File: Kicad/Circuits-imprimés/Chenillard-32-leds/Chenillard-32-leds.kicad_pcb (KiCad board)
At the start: 2 copper layers, 105 x 140 mm, 40 parts, among them J1 Conn_01x02, J2 Conn_01x02, J3 DB25_Female_MountingHoles, J4 DB25_Female_MountingHoles, U1 NE555, U2 4081, U3 4017, U4 4017, U5 4017, U6 4017

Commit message: Update PCB
Update routage and PCB hole mounting
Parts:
- added REF**: M3-Hole, Visserie-Trous-Modules:M3-Hole, F.Cu at (35.0, 40.0)
- added REF**: M3-Hole, Visserie-Trous-Modules:M3-Hole, F.Cu at (35.0, 170.0)
- added REF**: M3-Hole, Visserie-Trous-Modules:M3-Hole, F.Cu at (130.0, 170.0)
- added REF**: M3-Hole, Visserie-Trous-Modules:M3-Hole, F.Cu at (110.0, 50.0)
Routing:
- net RAZ: track 187.5 -> 219.6 mm
- net GND: track 588.8 -> 557.4 mm, vias 7 -> 5
- net Net-(U2-Pad11): track 66.6 -> 54.8 mm
- net Net-(U2-Pad8): track 87.4 -> 94.9 mm
- net +9V: track 428.1 -> 432.8 mm
- net Net-(U2-Pad10): track 58.1 -> 59.2 mm
- net Net-(J3-Pad1): track 44.8 -> 45.8 mm

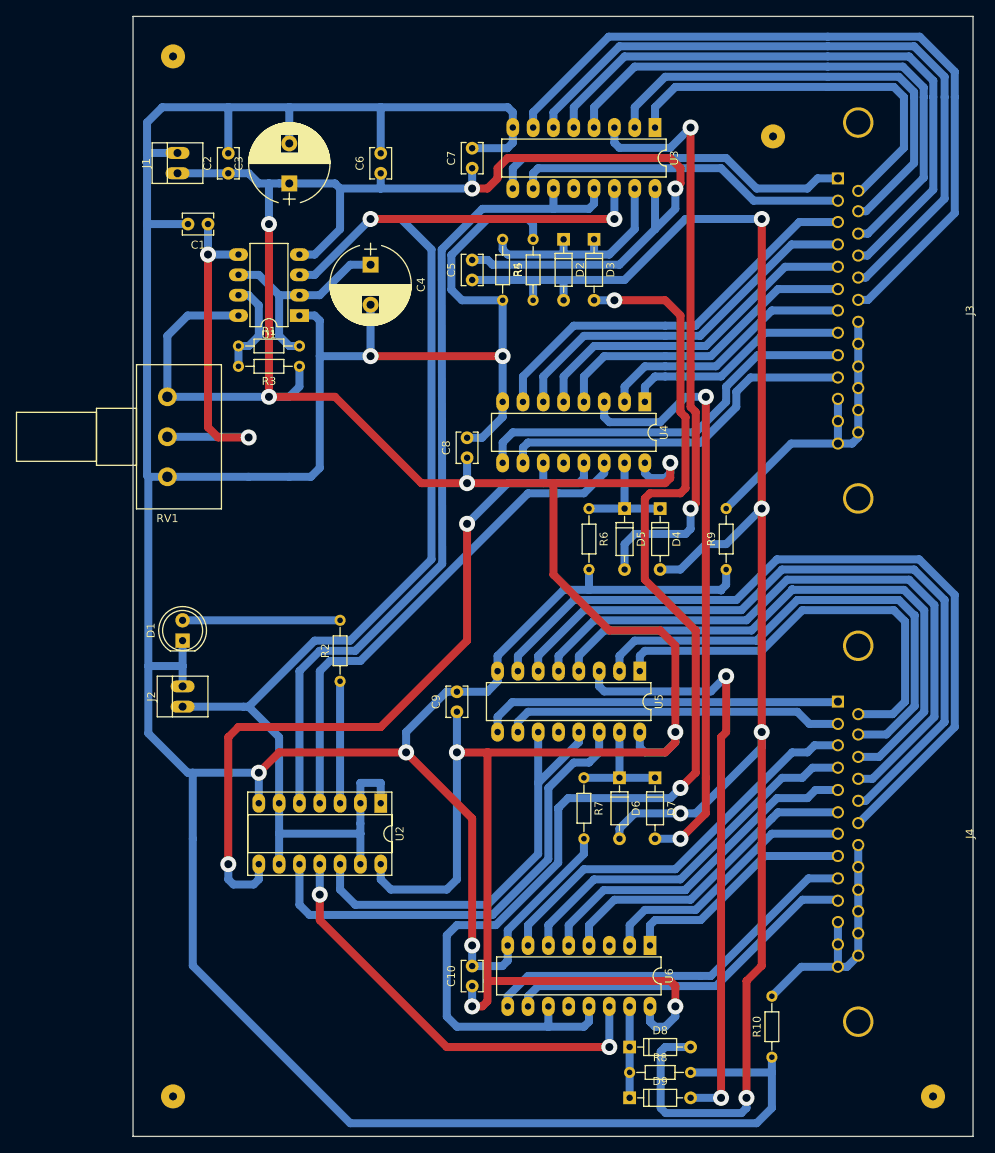
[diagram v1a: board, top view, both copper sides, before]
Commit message: Update project
Update project visual and mount facility components
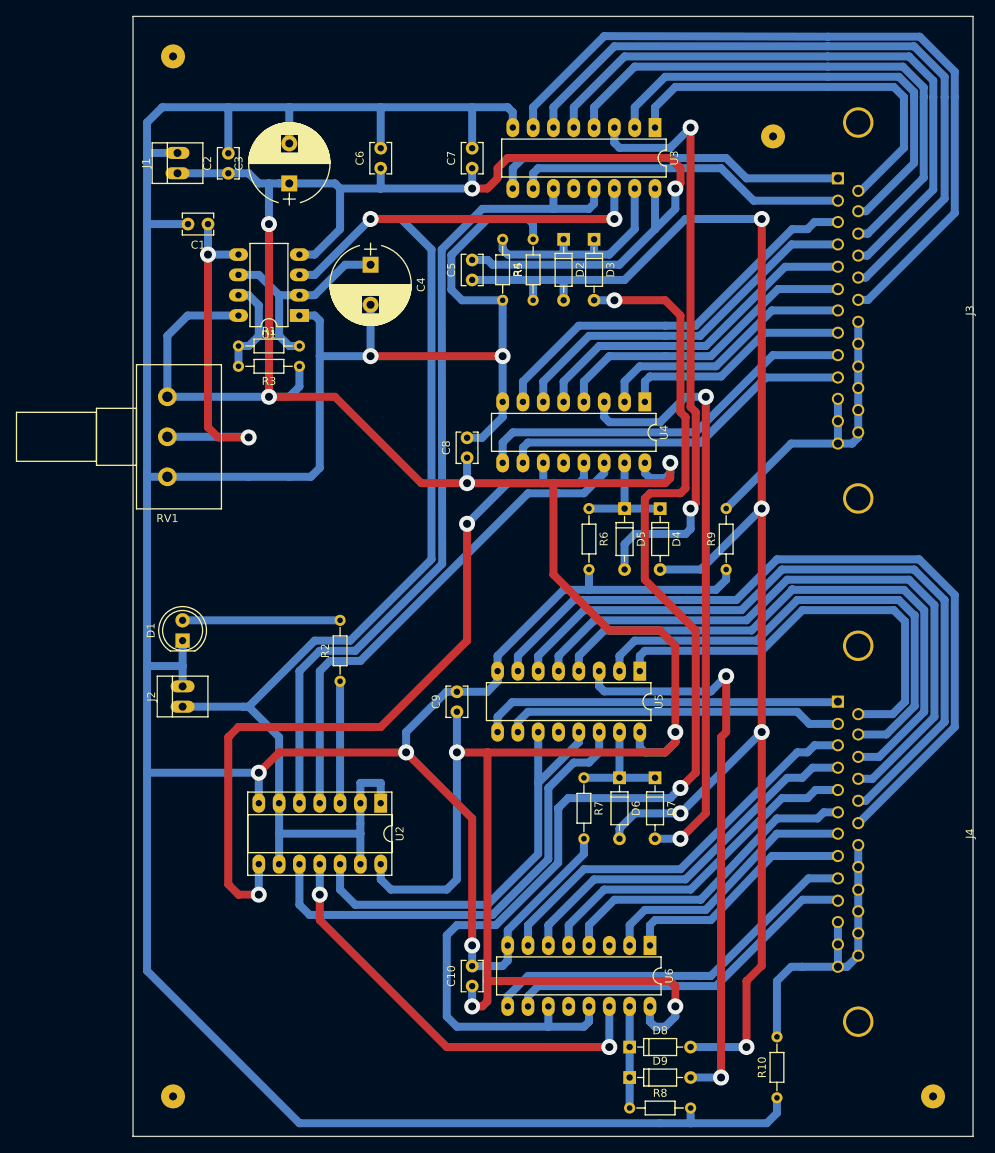
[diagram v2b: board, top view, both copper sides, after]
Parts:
- moved R10 5.12 mm to (110.5, 170.2)
- moved R8 4.44 mm to (92.1, 171.4)
- moved D9 2.54 mm to (92.1, 167.6)
- moved C6 0.63 mm to (61.0, 54.0)
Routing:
- net RAZ: track 219.6 -> 195.6 mm
- net GND: track 557.4 -> 551.4 mm
- net Net-(J4-Pad11): track 32.3 -> 38.0 mm
- net Net-(U2-Pad8): track 94.9 -> 97.4 mm
- net Net-(D9-Pad2): track 75.6 -> 73.1 mm
- net Net-(D8-Pad1): track 11.4 -> 12.7 mm
- net Net-(J3-Pad9): track 50.1 -> 49.0 mm
- net Net-(J3-Pad10): track 46.2 -> 45.1 mm
- net Net-(J3-Pad1): track 45.8 -> 44.8 mm
- net +9V: track 432.8 -> 433.4 mm
